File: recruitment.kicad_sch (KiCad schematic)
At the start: 1 part

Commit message: first setup: add ideas' text
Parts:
- removed C1: 1F, Capacitor_SMD:C_0805_2012Metric, symbol Device:C
- added K?: ADW11, Relay_THT:Relay_1P1T_NO_10x24x18.8mm_Panasonic_ADW11xxxxW_THT, symbol Relay:ADW11
- added U?: ACS781xLRTR-050B, Sensor_Current:Allegro_PSOF-7_4.8x6.4mm_P1.60mm, symbol Sensor_Current:ACS781xLRTR-050B
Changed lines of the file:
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@@
     (company "E-Agle TRT")
   )
-  (wire (pts (xy 199.39 121.92) (xy 193.04 121.92))
-    (stroke (width 0) (type default) (color 0 0 0 0))
-  )
-  (wire (pts (xy 193.04 121.92) (xy 193.04 130.81))
-    (stroke (width 0) (type default) (color 0 0 0 0))
-  )
-  (wire (pts (xy 199.39 130.81) (xy 199.39 129.54))
-    (stroke (width 0) (type default) (color 0 0 0 0))
-  )
-  (wire (pts (xy 193.04 130.81) (xy 199.39 130.81))
-    (stroke (width 0) (type default) (color 0 0 0 0))
-  )
-  (symbol (lib_id "Device:C") (at 199.39 125.73 0) (unit 1)
+  (symbol (lib_id "Sensor_Current:ACS781xLRTR-050B") (at 157.48 64.77 270) (unit 1)
     (in_bom yes) (on_board yes) (fields_autoplaced)
-    (property "Reference" "C1" (id 0) (at 203.2 124.4599 0)
-      (effects (font (size 1.27 1.27)) (justify left))
-    )
-    (property "Value" "1F" (id 1) (at 203.2 126.9999 0)
-      (effects (font (size 1.27 1.27)) (justify left))
-    )
-    (property "Footprint" "Capacitor_SMD:C_0805_2012Metric" (id 2) (at 200.3552 129.54 0)
+    (property "Reference" "U?" (id 0) (at 173.99 58.1912 90))
+    (property "Value" "ACS781xLRTR-050B" (id 1) (at 173.99 60.7312 90))
+    (property "Footprint" "Sensor_Current:Allegro_PSOF-7_4.8x6.4mm_P1.60mm" (id 2) (at 157.48 64.77 0)
       (effects (font (size 1.27 1.27)) hide)
     )
-    (property "Datasheet" "~" (id 3) (at 199.39 125.73 0)
+    (property "Datasheet" "http://www.allegromicro.com/~/media/Files/Datasheets/ACS780-Datasheet.ashx?la=en" (id 3) (at 157.48 64.77 0)
       (effects (font (size 1.27 1.27)) hide)
     )
     (pin "1")
     (pin "2")
+    (pin "3")
+    (pin "4")
+    (pin "5")
+    (pin "6")
+    (pin "7")
+  )
+  (symbol (lib_id "Relay:ADW11") (at 128.27 64.77 90) (unit 1)
+    (in_bom yes) (on_board yes) (fields_autoplaced)
+    (property "Reference" "K?" (id 0) (at 128.27 49.53 90))
+    (property "Value" "ADW11" (id 1) (at 128.27 52.07 90))
+    (property "Footprint" "Relay_THT:Relay_1P1T_NO_10x24x18.8mm_Panasonic_ADW11xxxxW_THT" (id 2) (at 129.54 31.115 0)
+      (effects (font (size 1.27 1.27)) hide)
+    )
+    (property "Datasheet" "https://www.panasonic-electric-works.com/pew/es/downloads/ds_dw_hl_en.pdf" (id 3) (at 128.27 64.77 0)
+      (effects (font (size 1.27 1.27)) hide)
+    )
+    (pin "1")
+    (pin "3")
+    (pin "5")
+    (pin "6")
   )
   (sheet_instances
@@
   )
   (symbol_instances
-    (path "/34d03349-6d78-4165-a683-2d8b76f2bae8"
-      (reference "C1") (unit 1) (value "1F") (footprint "Capacitor_SMD:C_0805_2012Metric")
+    (path "/b4450c83-6da6-4393-a892-92bf8cbec8aa"
+      (reference "K?") (unit 1) (value "ADW11") (footprint "Relay_THT:Relay_1P1T_NO_10x24x18.8mm_Panasonic_ADW11xxxxW_THT")
+    )
+    (path "/1b77c8f9-b0fa-45ba-a726-522a68924cf1"
+      (reference "U?") (unit 1) (value "ACS781xLRTR-050B") (footprint "Sensor_Current:Allegro_PSOF-7_4.8x6.4mm_P1.60mm")
     )
   )

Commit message: first circuit, TODO: check properly the voltage and the power
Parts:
- added Q? (x2): Q_NPN_BCE, symbol Device:Q_NPN_BCE
- added R? (x2): R, symbol Device:R
- added U? (x2): LM393, symbol Comparator:LM393
- added U?: LM7805_TO220, Package_TO_SOT_THT:TO-220-3_Vertical, symbol Regulator_Linear:LM7805_TO220
- K?: value ADW11 -> relay
- U?: value ACS781xLRTR-050B -> Hall effect sensor
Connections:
- net at U?.1 (VCC): now also Q?.3 (E), R?.1, R?.2, U?.2 (-)
- net GND: now reaches U?.2 (GND)
- net GND: now also K?.6, Q?.2 (C), Q?.3 (E), R?.2, U?.2 (GND), U?.4 (V-)
- net at U?.3 (VOUT): now also U?.3 (+)
- net at U?.6 (IP-): now also K?.5
- net at K?.1: now also Q?.2 (C), R?.1, U?.3 (VO)
- new net: Q?.1 (B), Q?.1 (B), U?.1

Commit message: setup for the win
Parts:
- regolator: renamed from U?; value LM7805_TO220 -> 5V
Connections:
- net at Q?.3 (E), R?.1, R?.2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: no longer U?.1 (VCC)
- net at U?.3 (VOUT): no longer U?.3 (+)
- net at K?.1, Q?.2 (C), R?.1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: now also U?.1 (VCC)
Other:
- moved on the sheet: Q?, R?, U?A, U?C

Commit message: ad633 imported
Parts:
- added U?: AD633JN, Analog_Devices-AD633JN-*, symbol eec:AD633JN
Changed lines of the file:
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@@
     (pin "7")
+  )
+  (symbol (lib_id "eec:AD633JN") (at 201.93 77.47 0) (unit 1)
+    (in_bom yes) (on_board yes) (fields_autoplaced)
+    (property "Reference" "U?" (id 0) (at 214.63 69.85 0))
+    (property "Value" "AD633JN" (id 1) (at 214.63 72.39 0))
+    (property "Footprint" "Analog_Devices-AD633JN-*" (id 2) (at 201.93 67.31 0)
+      (effects (font (size 1.27 1.27)) (justify left) hide)
+    )
+    (property "Datasheet" "http://www.analog.com/media/en/technical-documentation/data-sheets/AD633.pdf" (id 3) (at 201.93 64.77 0)
+      (effects (font (size 1.27 1.27)) (justify left) hide)
+    )
+    (property "Component Link 1 Description" "Manufacturer URL" (id 4) (at 201.93 62.23 0)
+      (effects (font (size 1.27 1.27)) (justify left) hide)
+    )
+    (property "Component Link 1 URL" "http://www.analog.com/en/index.html" (id 5) (at 201.93 59.69 0)
+      (effects (font (size 1.27 1.27)) (justify left) hide)
+    )
+    (property "Component Link 3 Description" "Package Specification" (id 6) (at 201.93 57.15 0)
+      (effects (font (size 1.27 1.27)) (justify left) hide)
+    )
+    (property "Component Link 3 URL" "http://www.analog.com/static/imported-files/packages/PKG_PDF/PDIP(N)/N_8.pdf" (id 7) (at 201.93 54.61 0)
+      (effects (font (size 1.27 1.27)) (justify left) hide)
+    )
+    (property "Datasheet Version" "Rev. K" (id 8) (at 201.93 52.07 0)
+      (effects (font (size 1.27 1.27)) (justify left) hide)
+    )
+    (property "Mounting Technology" "Through Hole" (id 9) (at 201.93 49.53 0)
+      (effects (font (size 1.27 1.27)) (justify left) hide)
+    )
+    (property "Number of Channels" "2" (id 10) (at 201.93 46.99 0)
+      (effects (font (size 1.27 1.27)) (justify left) hide)
+    )
+    (property "Package Description" "8-Pin Plastic Dual In-Line Package, Body 9.59 x 6.6 mm, Pitch 2.54 mm" (id 11) (at 201.93 44.45 0)
+      (effects (font (size 1.27 1.27)) (justify left) hide)
+    )
+    (property "Package Version" "07/2006" (id 12) (at 201.93 41.91 0)
+      (effects (font (size 1.27 1.27)) (justify left) hide)
+    )
+    (property "Packing" "Tube" (id 13) (at 201.93 39.37 0)
+      (effects (font (size 1.27 1.27)) (justify left) hide)
+    )
+    (property "Slew Rate" "20 V/us" (id 14) (at 201.93 36.83 0)
+      (effects (font (size 1.27 1.27)) (justify left) hide)
+    )
+    (property "Supply Current Max" "6 mA" (id 15) (at 201.93 34.29 0)
+      (effects (font (size 1.27 1.27)) (justify left) hide)
+    )
+    (property "Temperature Max" "70 degC" (id 16) (at 201.93 31.75 0)
+      (effects (font (size 1.27 1.27)) (justify left) hide)
+    )
+    (property "Temperature Min" "0 degC" (id 17) (at 201.93 29.21 0)
+      (effects (font (size 1.27 1.27)) (justify left) hide)
+    )
+    (property "category" "IC" (id 18) (at 201.93 26.67 0)
+      (effects (font (size 1.27 1.27)) (justify left) hide)
+    )
+    (property "library id" "82579f909b82c26c" (id 19) (at 201.93 24.13 0)
+      (effects (font (size 1.27 1.27)) (justify left) hide)
+    )
+    (property "manufacturer" "Analog Devices" (id 20) (at 201.93 21.59 0)
+      (effects (font (size 1.27 1.27)) (justify left) hide)
+    )
+    (property "package" "MS-001" (id 21) (at 201.93 19.05 0)
+      (effects (font (size 1.27 1.27)) (justify left) hide)
+    )
+    (property "vault revision" "D70804D2-C31E-4A78-88FF-EDD09AD4FF7C" (id 22) (at 201.93 16.51 0)
+      (effects (font (size 1.27 1.27)) (justify left) hide)
+    )
+    (property "imported" "yes" (id 23) (at 201.93 13.97 0)
+      (effects (font (size 1.27 1.27)) (justify left) hide)
+    )
+    (pin "1")
+    (pin "2")
+    (pin "3")
+    (pin "4")
+    (pin "5")
+    (pin "6")
+    (pin "7")
+    (pin "8")
   )
   (symbol (lib_id "Device:R") (at 142.24 100.33 90) (unit 1)
@@
       (reference "U?") (unit 1) (value "Hall effect sensor") (footprint "Sensor_Current:Allegro_PSOF-7_4.8x6.4mm_P1.60mm")
     )
+    (path "/394656a1-8b92-4995-815f-d107d37664e0"
+      (reference "U?") (unit 1) (value "AD633JN") (footprint "Analog_Devices-AD633JN-*")
+    )
     (path "/e6e45776-f57c-4519-a99b-28f22f45c493"

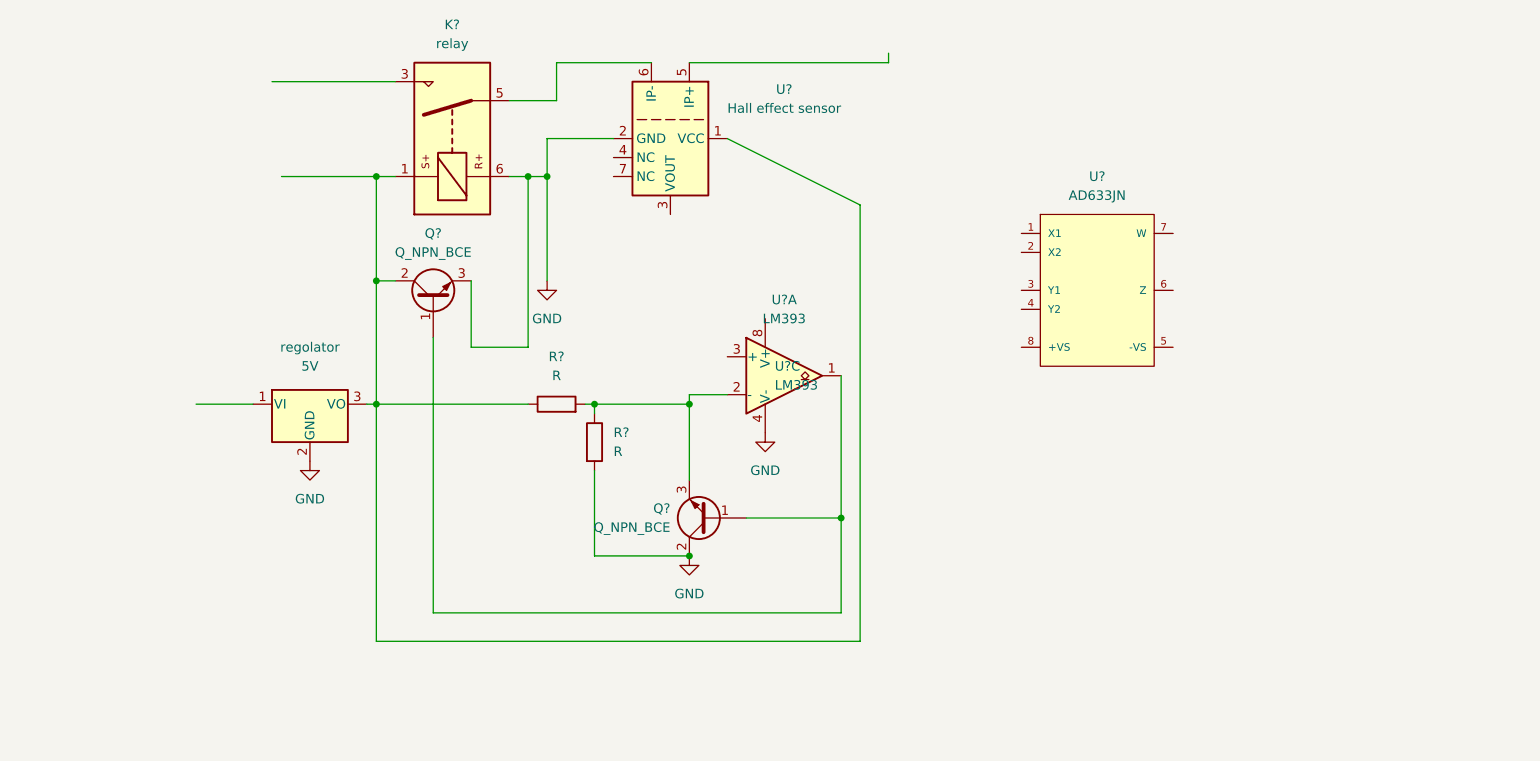
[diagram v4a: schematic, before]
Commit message: added AD633, TODO: do it in a better shape; add values
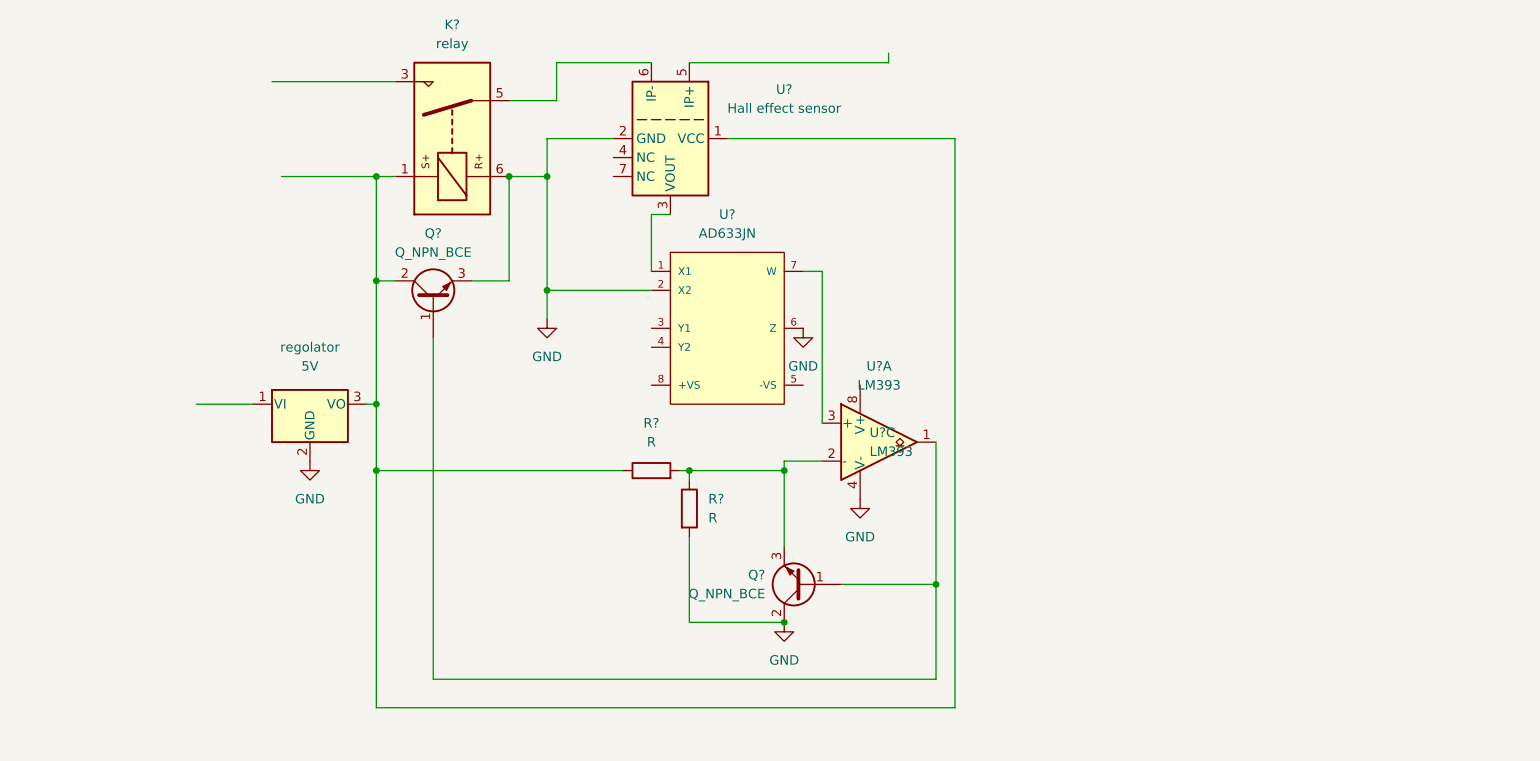
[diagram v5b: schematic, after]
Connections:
- net GND: now also U?.2 (X2), U?.6 (Z)
- net at U?.3 (VOUT): now also U?.1 (X1)
- net at U?.7 (W): now also U?.3 (+)
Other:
- moved on the sheet: Q?, R?, U?, U?A, U?C
